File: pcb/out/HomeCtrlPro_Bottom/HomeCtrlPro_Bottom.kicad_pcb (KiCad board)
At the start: 2 copper layers, 280 x 185 mm, 140 parts, among them J1 B2B, J10 OUT6, J11 OUT7, J12 OUTDC8, J13 OUTDC9, J14 OUTDC10, J15 OUTDC11, J16 OUTDC12, J17 OUTDC13, J18 OUTDC14, J19 OUTDC15, J2 24V, J3 230V, J4 OUT0, J5 OUT1, J6 OUT2, J7 OUT3, J8 OUT4, J9 OUT5, K1 SRD-24V, K2 SRD-24V, K3 SRD-24V, K4 SRD-24V, K5 SRD-24V, K6 SRD-24V, K7 SRD-24V, K8 SRD-24V, Q1 BC547, Q10 IRLZ44N, Q11 IRLZ44N, Q12 IRLZ44N, Q13 IRLZ44N, Q14 IRLZ44N, Q15 IRLZ44N, Q16 IRLZ44N, Q2 BC547, Q3 BC547, Q4 BC547, Q5 BC547, Q6 BC547, Q7 BC547, Q8 BC547, Q9 IRLZ44N, U1 MP1584, U2 AMS1117-3.3, U3 MCP23017

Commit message: ESP32-S3 + przyciski TFT; kompaktowy layout (szerokosc z liczby zlacz, 2 rzedy)
- Przejscie ESP32-C3 -> ESP32-S3 (duzo GPIO): niezalezne RS485/CAN, dotyk z IRQ,
  4 przyciski nawigacji TFT (GORA/DOL/OK/WSTECZ). Nowa czesc ESP32-S3-WROOM-1.
- Layout: I/O wzdluz krawedzi w 2 rzedach (podwojne w pionie), szerokosc plytki
  wynika z LICZBY zlacz (zmienne szerokosci kolumn) - wejscia na gornej krawedzi,
  wyjscia (zaciski) na dolnej. auto_frame() dobiera ciasna wspolna ramke.
- Przekazniki pakowane w strefe 230V (kilka rzedow) omijajaca otwory.
- HomeCtrlPro: 280x185 -> 168x192 mm, mniej pustego miejsca. Oba 0/0/0.

Testy 12/12, zwalidowane kiutils. Bloki: esp32s3, button.

Co-Authored-By: Claude Opus 4.8 (1M context) <noreply@anthropic.com>
Claude-Session: https://claude.ai/code/session_01LNGxtK2Jv1rJLBLPTwFQ9C
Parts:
- moved D16 257.3 mm to (14.2, 58.8)
- moved R35 256.8 mm to (9.10, 58.2)
- moved R34 256.3 mm to (5.20, 58.2)
- moved J19 206.0 mm to (129.1, 176.2), turned to 180 degrees
- moved J18 201.6 mm to (129.1, 186.3), turned to 180 degrees
- moved K8 195.4 mm to (48.0, 142.2)
- moved J16 187.6 mm to (115.9, 186.3), turned to 180 degrees
- moved J17 186.9 mm to (115.9, 176.2), turned to 180 degrees
- moved K7 186.5 mm to (27.5, 142.2)
- moved LED5 183.0 mm to (80.8, 46.0)
- moved J12 182.9 mm to (89.6, 186.3), turned to 180 degrees
- moved D7 182.5 mm to (75.8, 46.6)
- moved R11 182.1 mm to (70.7, 46.0)
- moved Q5 181.6 mm to (66.4, 46.7)
- moved J14 181.1 mm to (102.7, 186.3), turned to 180 degrees
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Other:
- board size 280 x 185 mm -> 168 x 191.8 mm

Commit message: Wejscia w jednym rzedzie PRZY krawedzi + gniazda RJ45 podwojne (2 porty w pionie)
Poprawka po blednej interpretacji: I/O ustawiane w JEDNYM rzedzie zlicowanym do
krawedzi (koniec ze stosowaniem zlacz w 2 rzedach do wnetrza). Szerokosc plytki
= suma szerokosci zlacz w rzedzie. Nowa czesc RJ45_Dual (2 porty RJ45 w jednej
obudowie, jeden nad drugim) + blok input_bank_dual (8 wejsc/gniazdo, TVS/wejscie).
HomeCtrlPro: 4 podwojne RJ45 = 32 wejscia. Oba PCB 0/0/0, testy 12/12, kiutils OK.

Co-Authored-By: Claude Opus 4.8 (1M context) <noreply@anthropic.com>
Claude-Session: https://claude.ai/code/session_01LNGxtK2Jv1rJLBLPTwFQ9C
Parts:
- moved LED3 149.9 mm to (182.3, 15.4)
- moved R10 149.9 mm to (208.8, 15.4)
- moved R9 149.9 mm to (194.8, 15.4)
- moved LED4 149.9 mm to (204.9, 15.4)
- moved LED5 149.9 mm to (227.5, 15.4)
- moved R11 149.9 mm to (217.4, 15.4)
- moved R12 149.9 mm to (231.4, 15.4)
- moved R6 149.9 mm to (163.6, 15.4)
- moved R7 149.9 mm to (172.2, 15.4)
- moved R8 149.9 mm to (186.2, 15.4)
- moved Q3 149.8 mm to (167.9, 16.2)
- moved D5 149.8 mm to (177.2, 16.1)
- moved D6 149.8 mm to (199.8, 16.1)
- moved D7 149.8 mm to (222.4, 16.1)
- moved Q4 149.8 mm to (190.5, 16.2)
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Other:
- board size 168 x 191.8 mm -> 237.4 x 152.8 mm

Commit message: Wiecej RJ45 (8 podwojnych=64 wej), zabezpieczenia, zlacza na obu krawedziach
- Wejscia: 8 podwojnych RJ45 = 16 portow = 64 wejscia (4 ekspandery MCP23017).
- Zabezpieczenia: PTC na kazde z 16 wyjsc, MOV na wyjsciach 230V, snubber RC na
  stykach przekaznikow, dlawik wspolny (CMC) + TVS na RS485/CAN, TVS na wyjsciach DC.
  Nowe czesci: PTC (polyfuse), CMC (common-mode choke).
- Layout: zlacza rozlozone na GORNA i DOLNA krawedz (_split_balanced) -> wezsza
  plytka; gestsze upakowanie, mniejszy luz wysokosci. auto_frame liczy szerokosc
  z rozlozenia na 2 krawedzie. HomeCtrlPro: 237 -> 155 mm szerokosci.

Oba PCB 0/0/0, testy 12/12, kiutils OK.

Co-Authored-By: Claude Opus 4.8 (1M context) <noreply@anthropic.com>
Claude-Session: https://claude.ai/code/session_01LNGxtK2Jv1rJLBLPTwFQ9C
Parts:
- added C12: 100nF, pcbforge:C_0805, F.Cu at (23.1, 57.9)
- added C13: 100nF, pcbforge:C_0805, F.Cu at (69.1, 57.9)
- added C14: 100nF, pcbforge:C_0805, F.Cu at (115.1, 57.9)
- added C15: 100nF, pcbforge:C_0805, F.Cu at (13.0, 68.4)
- added C16: 100nF, pcbforge:C_0805, F.Cu at (59.0, 68.4)
- added C17: 100nF, pcbforge:C_0805, F.Cu at (105.0, 68.4)
- added C18: 100nF, pcbforge:C_0805, F.Cu at (5.20, 78.9)
- added C19: 100nF, pcbforge:C_0805, F.Cu at (51.2, 78.9)
- added D19: SS34, pcbforge:D_SMA, F.Cu at (100.5, 90.1)
- added D20: TVS, pcbforge:D_SOD-323, F.Cu at (118.7, 89.4)
- added D21: SS34, pcbforge:D_SMA, F.Cu at (139.7, 90.1)
- added D22: TVS, pcbforge:D_SOD-323, F.Cu at (10.6, 96.9)
- added D23: SS34, pcbforge:D_SMA, F.Cu at (31.6, 97.6)
- added D24: TVS, pcbforge:D_SOD-323, F.Cu at (49.8, 96.9)
- added D25: SS34, pcbforge:D_SMA, F.Cu at (70.8, 97.6)
- added D26: TVS, pcbforge:D_SOD-323, F.Cu at (89.0, 96.9)
- added F10: 2A, pcbforge:F_1206, F.Cu at (101.0, 79.1)
- added F11: 2A, pcbforge:F_1206, F.Cu at (140.2, 79.1)
- added F12: 2A, pcbforge:F_1206, F.Cu at (35.5, 89.6)
- added F13: 2A, pcbforge:F_1206, F.Cu at (74.7, 89.6)
- added F14: 2A, pcbforge:F_1206, F.Cu at (113.9, 89.6)
- added F15: 2A, pcbforge:F_1206, F.Cu at (5.80, 97.1)
- added F16: 2A, pcbforge:F_1206, F.Cu at (45.0, 97.1)
- added F17: 2A, pcbforge:F_1206, F.Cu at (84.2, 97.1)
- added F2: 0.5A, pcbforge:F_1206, F.Cu at (27.6, 58.1)
- added F3: 0.5A, pcbforge:F_1206, F.Cu at (73.6, 58.1)
- added F4: 0.5A, pcbforge:F_1206, F.Cu at (119.6, 58.1)
- added F5: 0.5A, pcbforge:F_1206, F.Cu at (17.5, 68.6)
- added F6: 0.5A, pcbforge:F_1206, F.Cu at (63.5, 68.6)
- added F7: 0.5A, pcbforge:F_1206, F.Cu at (109.5, 68.6)
- added F8: 0.5A, pcbforge:F_1206, F.Cu at (9.70, 79.1)
- added F9: 0.5A, pcbforge:F_1206, F.Cu at (55.7, 79.1)
- added R43: 100k, pcbforge:R_0805, F.Cu at (134.6, 89.4)
- added R44: 1k, pcbforge:R_0805, F.Cu at (148.6, 89.4)
- added R45: 100, pcbforge:R_0805, F.Cu at (22.6, 96.9)
- added R46: 100k, pcbforge:R_0805, F.Cu at (26.5, 96.9)
- added R47: 1k, pcbforge:R_0805, F.Cu at (40.5, 96.9)
- added R48: 100, pcbforge:R_0805, F.Cu at (61.8, 96.9)
- added R49: 100k, pcbforge:R_0805, F.Cu at (65.7, 96.9)
- added R50: 1k, pcbforge:R_0805, F.Cu at (79.7, 96.9)
- added RV2: S14K275, pcbforge:MOV_Disc, F.Cu at (35.4, 61.6)
- added RV3: S14K275, pcbforge:MOV_Disc, F.Cu at (81.4, 61.6)
- added RV4: S14K275, pcbforge:MOV_Disc, F.Cu at (127.4, 61.6)
- added RV5: S14K275, pcbforge:MOV_Disc, F.Cu at (25.3, 72.1)
- added RV6: S14K275, pcbforge:MOV_Disc, F.Cu at (71.3, 72.1)
- added RV7: S14K275, pcbforge:MOV_Disc, F.Cu at (117.3, 72.1)
- added RV8: S14K275, pcbforge:MOV_Disc, F.Cu at (17.5, 82.6)
- added RV9: S14K275, pcbforge:MOV_Disc, F.Cu at (63.5, 82.6)
- D12, D14, D16, D18: value SS34 -> TVS; footprint pcbforge:D_SMA -> pcbforge:D_SOD-323
- R11, R14, R17, R27, R30, R33, R36, R39, R42, R5, R8: value 1k -> 100
- R19, R22, R25: value 100 -> 1k
- R20, R23, R26: value 100k -> 100
- R28, R31, R34, R37, R40: value 100 -> 100k
- R29, R32, R35, R38, R41: value 100k -> 1k
- moved D15 203.2 mm to (22.1, 90.1)
- moved LED5 187.8 mm to (47.3, 68.4)
- moved D7 187.8 mm to (42.2, 69.1)
- moved Q5 187.8 mm to (32.9, 69.2)
- moved Q11 146.7 mm to (7.20, 91.6)
- moved LED11 146.7 mm to (27.1, 89.4)
- moved J10 145.4 mm to (131.9, 5.54), turned to 0 degrees
- moved J4 145.4 mm to (52.9, 5.54), turned to 0 degrees
- moved J5 145.4 mm to (66.1, 5.54), turned to 0 degrees
- moved J6 145.4 mm to (79.2, 5.54), turned to 0 degrees
- moved J7 145.4 mm to (92.4, 5.54), turned to 0 degrees
- moved J8 145.4 mm to (105.6, 5.54), turned to 0 degrees
- moved J9 145.4 mm to (118.7, 5.54), turned to 0 degrees
- moved LED12 137.9 mm to (66.3, 89.4)
- moved Q12 137.9 mm to (46.4, 91.6)
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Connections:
- D11 pad 1: OUT8 -> _DRN8
- D12 pad 1: OUT9 -> OUTDC8
- D12 pad 2: V24P -> GND
- D13 pad 1: OUT10 -> _DRN9
- D14 pad 1: OUT11 -> OUTDC9
- D14 pad 2: V24P -> GND
- D15 pad 1: OUT12 -> _DRN10
- D16 pad 1: OUT13 -> OUTDC10
- D16 pad 2: V24P -> GND
- D17 pad 1: OUT14 -> _DRN11
- D18 pad 1: OUT15 -> OUTDC11
- D18 pad 2: V24P -> GND
- J12 pad 2: OUT8 -> OUTDC8
- J13 pad 2: OUT9 -> OUTDC9
- J14 pad 2: OUT10 -> OUTDC10
- J15 pad 2: OUT11 -> OUTDC11
- J16 pad 2: OUT12 -> OUTDC12
- J17 pad 2: OUT13 -> OUTDC13
- J18 pad 2: OUT14 -> OUTDC14
- J19 pad 2: OUT15 -> OUTDC15
- K1 pad 3: LAMP0 -> _NO0
- K2 pad 3: LAMP1 -> _NO1
- K3 pad 3: LAMP2 -> _NO2
- K4 pad 3: LAMP3 -> _NO3
- K5 pad 3: LAMP4 -> _NO4
- K6 pad 3: LAMP5 -> _NO5
- K7 pad 3: LAMP6 -> _NO6
- K8 pad 3: LAMP7 -> _NO7
- Q10 pad 2: OUT9 -> _DRN9
- Q11 pad 2: OUT10 -> _DRN10
- Q12 pad 2: OUT11 -> _DRN11
- Q13 pad 2: OUT12 -> _DRN12
- Q14 pad 2: OUT13 -> _DRN13
- Q15 pad 2: OUT14 -> _DRN14
- Q16 pad 2: OUT15 -> _DRN15
- Q9 pad 2: OUT8 -> _DRN8
- R10 pad 1: OUT3 -> OUT2
- R10 pad 2: _RL3 -> _RL2
- R11 pad 1: OUT4 -> L
- R11 pad 2: _RB4 -> _SN2
- R12 pad 1: OUT4 -> OUT3
- R12 pad 2: _RL4 -> _RB3
- R13 pad 1: OUT5 -> OUT3
- R13 pad 2: _RB5 -> _RL3
- R14 pad 1: OUT5 -> L
- R14 pad 2: _RL5 -> _SN3
- R15 pad 1: OUT6 -> OUT4
- R15 pad 2: _RB6 -> _RB4
- R16 pad 1: OUT6 -> OUT4
- R16 pad 2: _RL6 -> _RL4
- R17 pad 1: OUT7 -> L
- R17 pad 2: _RB7 -> _SN4
- R18 pad 1: OUT7 -> OUT5
- R18 pad 2: _RL7 -> _RB5
- R19 pad 1: OUT8 -> OUT5
- R19 pad 2: _G8 -> _RL5
- R20 pad 1: _G8 -> L
- R20 pad 2: GND -> _SN5
- R21 pad 1: OUT8 -> OUT6
- R21 pad 2: _ML8 -> _RB6
- R22 pad 1: OUT9 -> OUT6
- R22 pad 2: _G9 -> _RL6
- R23 pad 1: _G9 -> L
- R23 pad 2: GND -> _SN6
- R24 pad 1: OUT9 -> OUT7
- R24 pad 2: _ML9 -> _RB7
- R25 pad 1: OUT10 -> OUT7
- R25 pad 2: _G10 -> _RL7
- R26 pad 1: _G10 -> L
- R26 pad 2: GND -> _SN7
- R27 pad 1: OUT10 -> OUT8
- R27 pad 2: _ML10 -> _G8
- R28 pad 1: OUT11 -> _G8
- R28 pad 2: _G11 -> GND
- R29 pad 1: _G11 -> OUT8
- R29 pad 2: GND -> _ML8
- R30 pad 1: OUT11 -> OUT9
- R30 pad 2: _ML11 -> _G9
- R31 pad 1: OUT12 -> _G9
- R31 pad 2: _G12 -> GND
- R32 pad 1: _G12 -> OUT9
- R32 pad 2: GND -> _ML9
- R33 pad 1: OUT12 -> OUT10
- R33 pad 2: _ML12 -> _G10
- R34 pad 1: OUT13 -> _G10
- R34 pad 2: _G13 -> GND
- R35 pad 1: _G13 -> OUT10
- R35 pad 2: GND -> _ML10
- R36 pad 1: OUT13 -> OUT11
- R36 pad 2: _ML13 -> _G11
- R37 pad 1: OUT14 -> _G11
- R37 pad 2: _G14 -> GND
- R38 pad 1: _G14 -> OUT11
- R38 pad 2: GND -> _ML11
- R39 pad 1: OUT14 -> OUT12
- R39 pad 2: _ML14 -> _G12
- R40 pad 1: OUT15 -> _G12
- R40 pad 2: _G15 -> GND
- R41 pad 1: _G15 -> OUT12
- R41 pad 2: GND -> _ML12
- R42 pad 1: OUT15 -> OUT13
- R42 pad 2: _ML15 -> _G13
- R5 pad 1: OUT1 -> L
- R5 pad 2: _RB1 -> _SN0
- R6 pad 2: _RL1 -> _RB1
- R7 pad 1: OUT2 -> OUT1
- R7 pad 2: _RB2 -> _RL1
- R8 pad 1: OUT2 -> L
- R8 pad 2: _RL2 -> _SN1
- R9 pad 1: OUT3 -> OUT2
- R9 pad 2: _RB3 -> _RB2
- U3 pad 16: 3V3 -> GND
- U3 pad 17: GND -> 3V3
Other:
- board size 237.4 x 152.8 mm -> 155.4 x 230.2 mm

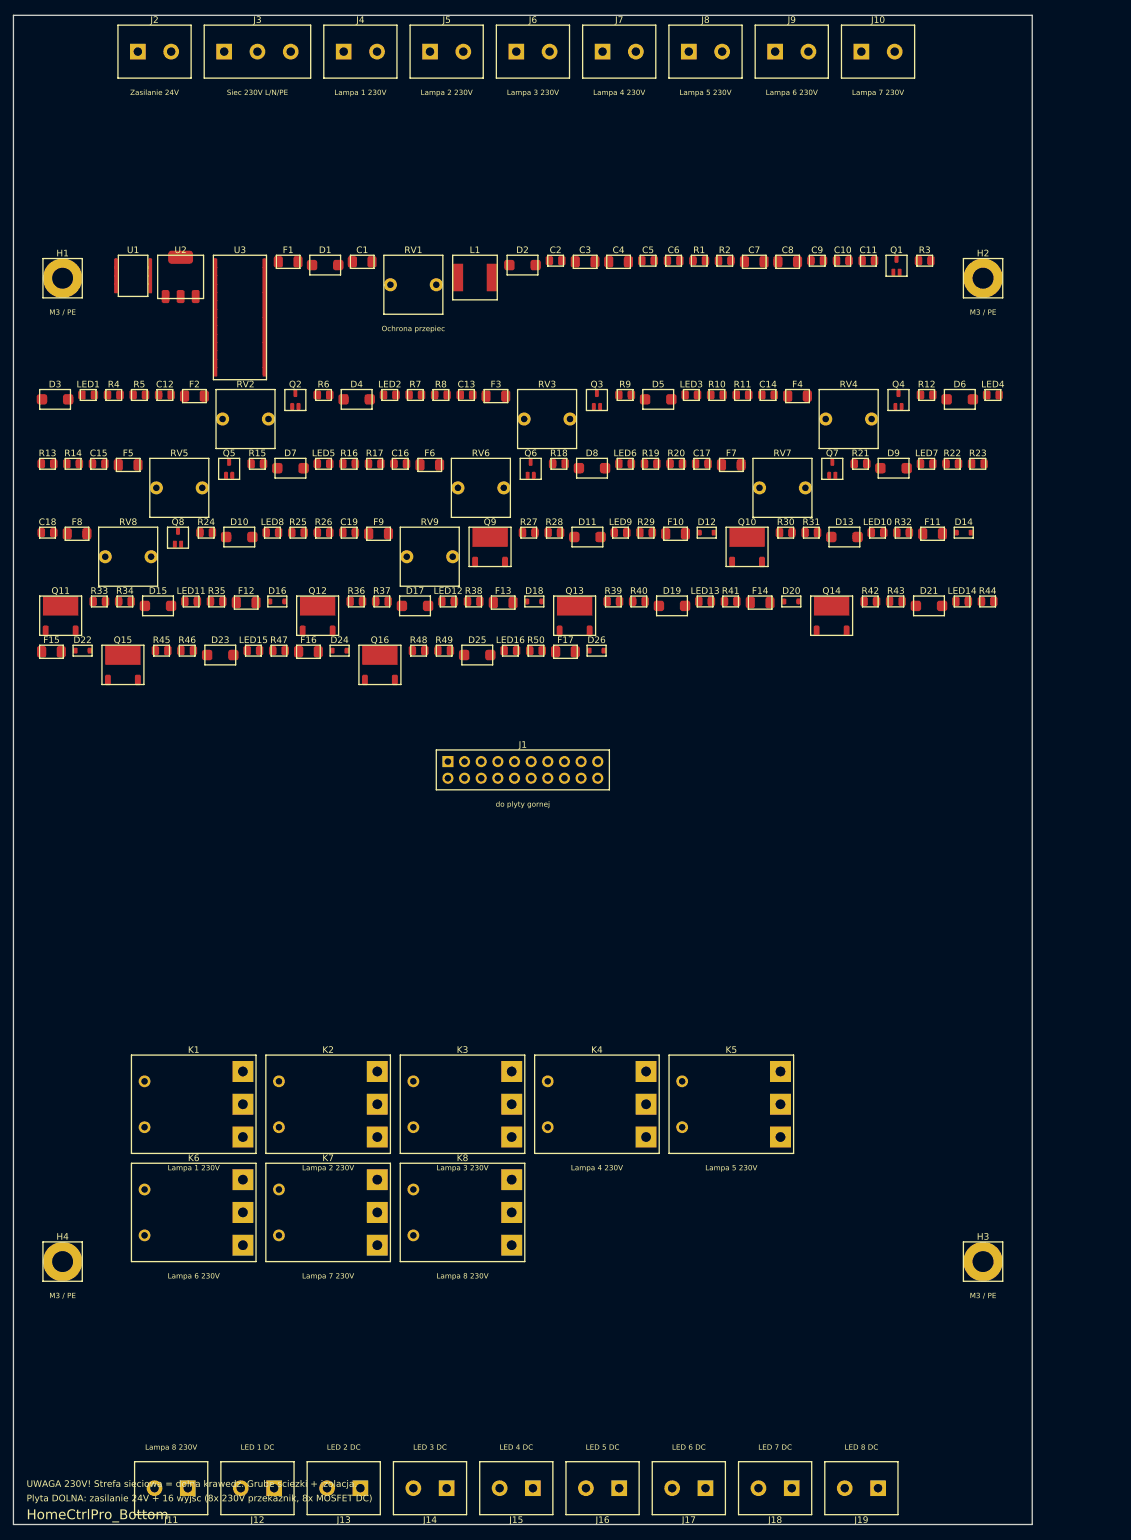
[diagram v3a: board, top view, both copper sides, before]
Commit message: Zageszczenie layoutu: ~2x mniejsza plytka (zajetosc 18% -> 38%)
- Pakowanie sortowane po wysokosci (wiersze o zblizonej wysokosci) - koniec z
  marnowaniem miejsca przez wysoki element w rzedzie.
- io_band = male wciecie (nie wysokosc zlacza); wysokie podwojne RJ45 mieszcza
  sie w srodku, nie rozdmuchuja pasow krawedziowych.
- Niezalezne wysokosci plyt (auto_layout) przy WSPOLNYCH otworach i B2B - mniejsza
  plyta nie dziedziczy wysokosci wiekszej.
- Wnetrze + przekazniki jako jeden ciasny blok; szerokosc wnetrza w estymacie =
  rzeczywista (koniec z przeszacowana wysokoscia/luka).
- Wysokie zlacza grupowane na jedna krawedz; TFT 2x07 (polowa szerokosci).

HomeCtrlPro DOL: 280x185 -> 168x100 mm. Oba 0/0/0, testy 12/12, kiutils OK.

Co-Authored-By: Claude Opus 4.8 (1M context) <noreply@anthropic.com>
Claude-Session: https://claude.ai/code/session_01LNGxtK2Jv1rJLBLPTwFQ9C
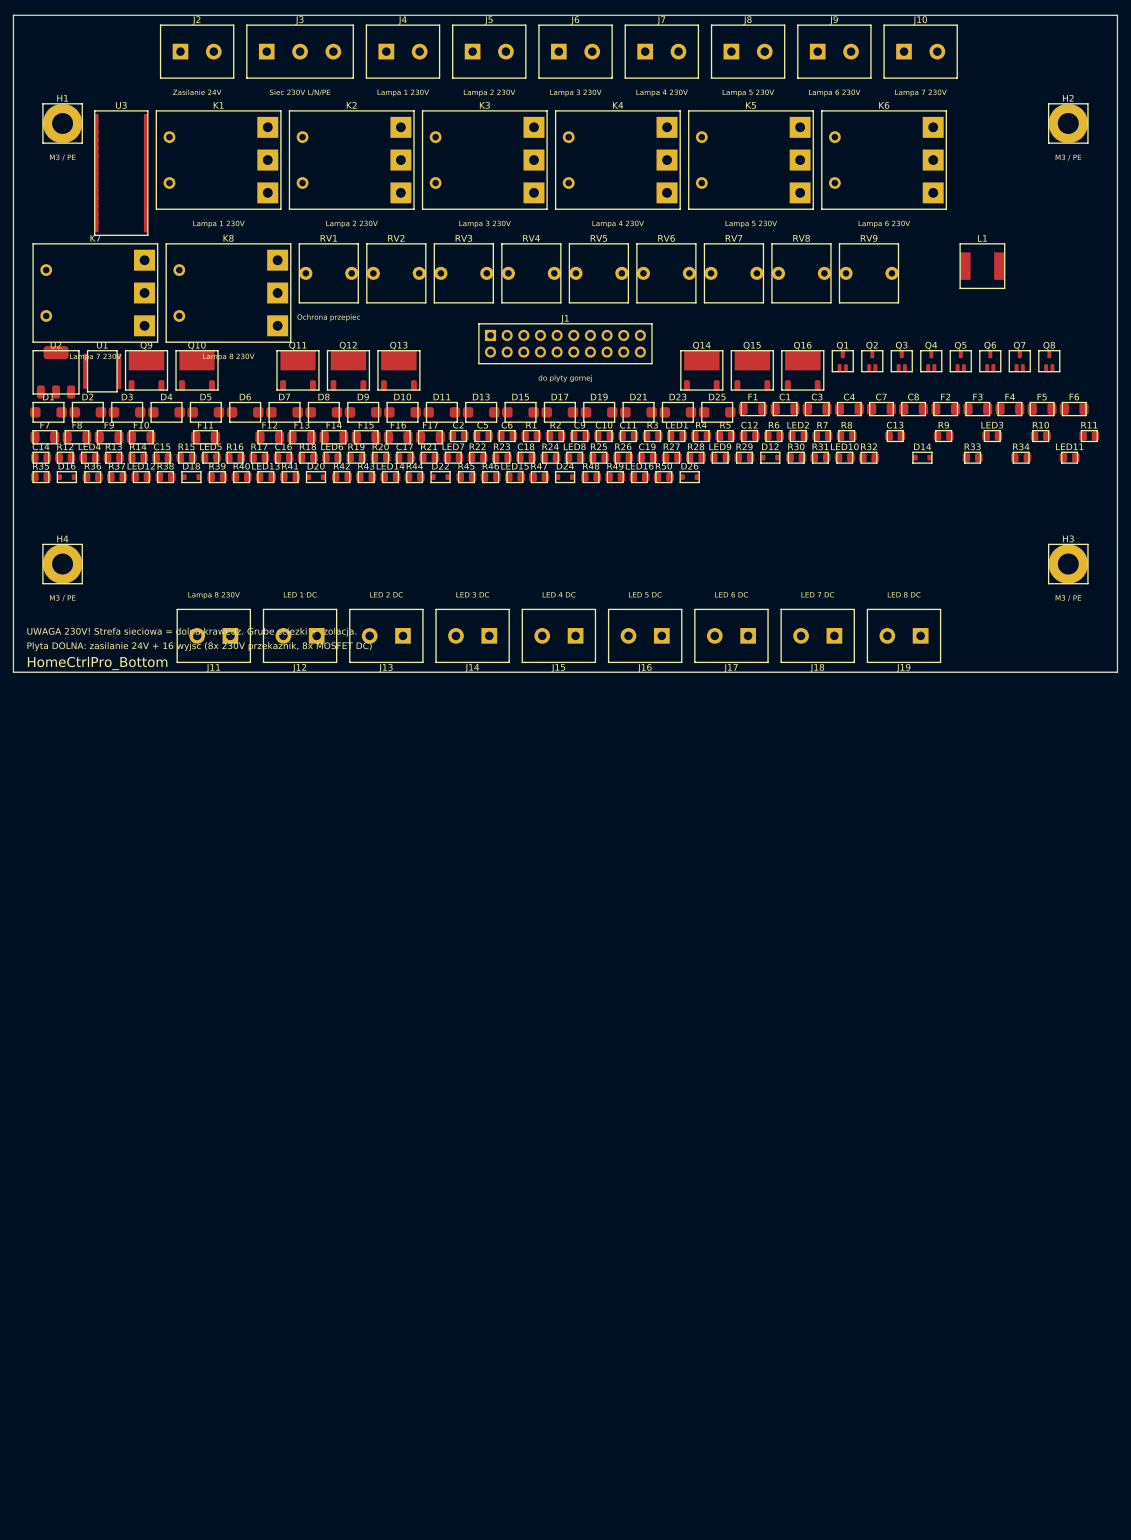
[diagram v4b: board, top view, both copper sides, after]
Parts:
- moved K6 192.0 mm to (132.8, 22.1)
- moved K8 144.7 mm to (32.8, 42.4)
- moved K7 144.7 mm to (12.5, 42.4)
- moved K1 144.1 mm to (31.3, 22.1)
- moved K2 144.1 mm to (51.6, 22.1)
- moved K3 144.1 mm to (71.9, 22.1)
- moved K4 144.1 mm to (92.2, 22.1)
- moved K5 144.1 mm to (112.5, 22.1)
- moved F5 139.7 mm to (156.9, 60.1)
- moved R34 138.4 mm to (153.7, 67.5)
- moved LED4 138.1 mm to (11.6, 67.5)
- moved LED11 135.8 mm to (161.1, 67.5)
- moved Q8 135.6 mm to (158.0, 52.8)
- moved R33 135.0 mm to (146.3, 67.5)
- moved R12 131.7 mm to (7.90, 67.5)
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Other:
- board size 155.4 x 230.2 mm -> 168.4 x 100.2 mm
